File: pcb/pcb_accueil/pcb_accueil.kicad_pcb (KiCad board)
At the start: 2 copper layers, 76 x 32 mm, 5 parts, among them J1 AMP 5- 5530843-4, J2 IDC - Header 2x10

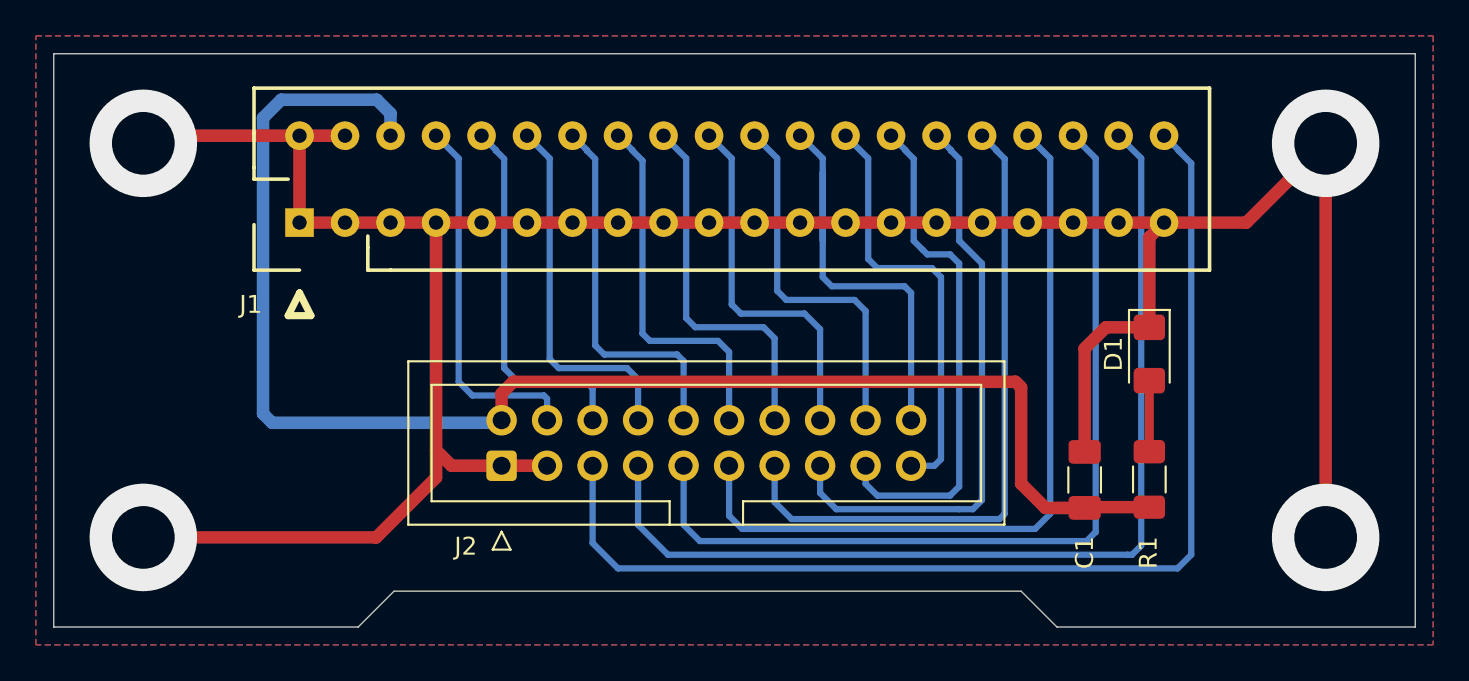
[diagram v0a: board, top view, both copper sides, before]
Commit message: rajout de trous de precage dans pcb_accueil
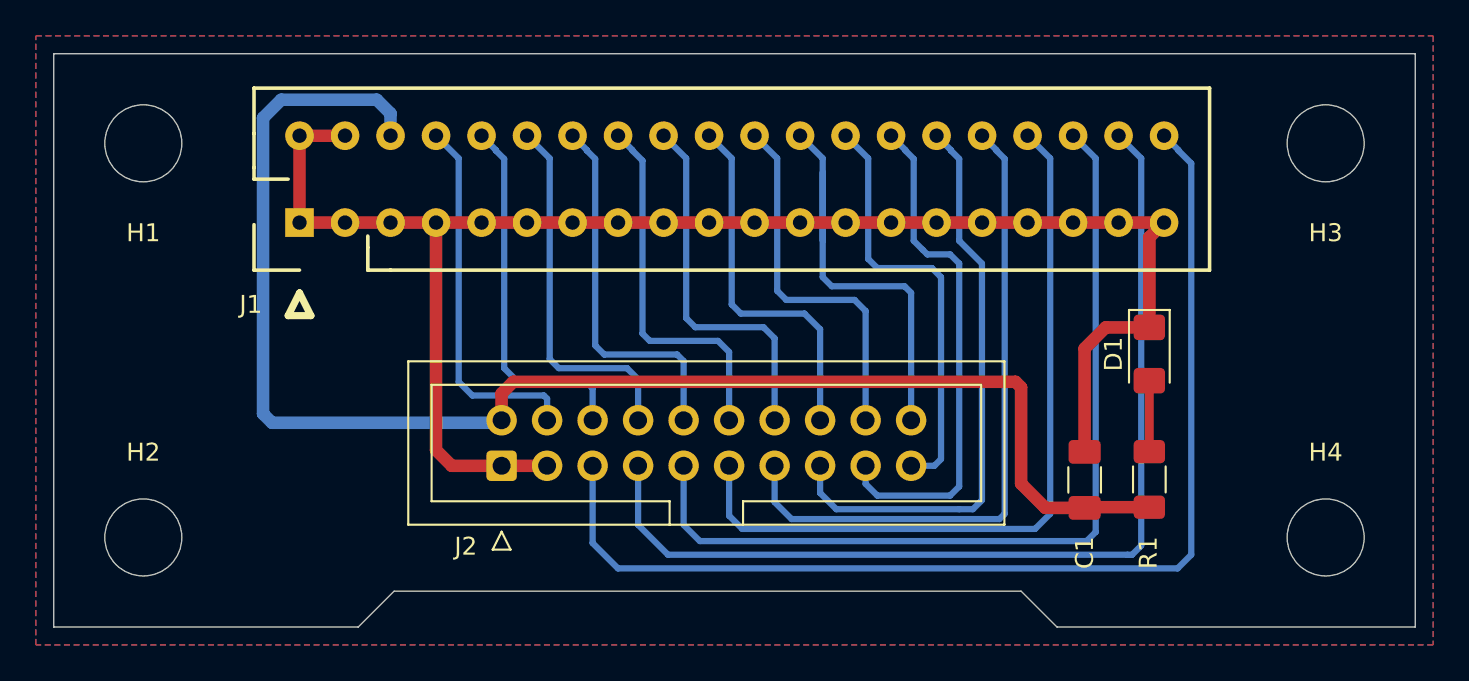
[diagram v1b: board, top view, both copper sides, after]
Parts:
- added H1: MountingHole, MountingHole:MountingHole_4.3mm_M4_DIN965, F.Cu at (116.0, 86.0)
- added H2: MountingHole, MountingHole:MountingHole_4.3mm_M4_DIN965, F.Cu at (116.0, 108.0)
- added H3: MountingHole, MountingHole:MountingHole_4.3mm_M4_DIN965, F.Cu at (182.0, 86.0)
- added H4: MountingHole, MountingHole:MountingHole_4.3mm_M4_DIN965, F.Cu at (182.0, 108.0)
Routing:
- net GND: track 152.0 -> 91.0 mm, vias 4 -> 0
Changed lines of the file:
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@@
     (thickness 1.6)
     (drawings 16)
-    (tracks 170)
+    (tracks 158)
     (zones 0)
-    (modules 5)
+    (modules 9)
     (nets 21)
   )
@@
   )
   (setup
-    (last_trace_width 0.7)
+    (last_trace_width 0.25)
     (user_trace_width 0.25)
     (user_trace_width 0.3)
@@
     (mod_text_size 1 1)
     (mod_text_width 0.15)
-    (pad_size 1.524 1.524)
-    (pad_drill 0.762)
+    (pad_size 4.3 4.3)
+    (pad_drill 4.3)
     (pad_to_mask_clearance 0.051)
     (solder_mask_min_width 0.25)
@@
     )
   )
+  (module MountingHole:MountingHole_4.3mm_M4_DIN965 locked (layer F.Cu)
+    (at 116 86)
+    (descr "Mounting Hole 4.3mm, no annular, M4, DIN965")
+    (tags "mounting hole 4.3mm no annular m4 din965")
+    (attr virtual)
+    (fp_text reference H1 (at 0 5) (layer F.SilkS)
+      (effects (font (size 1 1) (thickness 0.15)))
+    )
+    (fp_text value MountingHole (at 0 4.75) (layer F.Fab)
+      (effects (font (size 1 1) (thickness 0.15)))
+    )
+    (fp_text user %R (at 0.3 0) (layer F.Fab)
+      (effects (font (size 1 1) (thickness 0.15)))
+    )
+    (fp_circle (center 0 0) (end 3.75 0) (layer Cmts.User) (width 0.15))
+    (fp_circle (center 0 0) (end 4 0) (layer F.CrtYd) (width 0.05))
+    (pad 1 np_thru_hole circle (at 0 0) (size 4.3 4.3) (drill 4.3) (layers *.Cu *.Mask))
+  )
+  (module MountingHole:MountingHole_4.3mm_M4_DIN965 locked (layer F.Cu)
+    (at 116 108)
+    (descr "Mounting Hole 4.3mm, no annular, M4, DIN965")
+    (tags "mounting hole 4.3mm no annular m4 din965")
+    (attr virtual)
+    (fp_text reference H2 (at 0 -4.75) (layer F.SilkS)
+      (effects (font (size 1 1) (thickness 0.15)))
+    )
+    (fp_text value MountingHole (at 0 4.75) (layer F.Fab)
+      (effects (font (size 1 1) (thickness 0.15)))
+    )
+    (fp_circle (center 0 0) (end 4 0) (layer F.CrtYd) (width 0.05))
+    (fp_circle (center 0 0) (end 3.75 0) (layer Cmts.User) (width 0.15))
+    (fp_text user %R (at 0.3 0) (layer F.Fab)
+      (effects (font (size 1 1) (thickness 0.15)))
+    )
+    (pad 1 np_thru_hole circle (at 0 0) (size 4.3 4.3) (drill 4.3) (layers *.Cu *.Mask))
+  )
+  (module MountingHole:MountingHole_4.3mm_M4_DIN965 locked (layer F.Cu)
+    (at 182 86)
+    (descr "Mounting Hole 4.3mm, no annular, M4, DIN965")
+    (tags "mounting hole 4.3mm no annular m4 din965")
+    (attr virtual)
+    (fp_text reference H3 (at 0 5) (layer F.SilkS)
+      (effects (font (size 1 1) (thickness 0.15)))
+    )
+    (fp_text value MountingHole (at 0 4.75) (layer F.Fab)
+      (effects (font (size 1 1) (thickness 0.15)))
+    )
+    (fp_text user %R (at 0.3 0) (layer F.Fab)
+      (effects (font (size 1 1) (thickness 0.15)))
+    )
+    (fp_circle (center 0 0) (end 3.75 0) (layer Cmts.User) (width 0.15))
+    (fp_circle (center 0 0) (end 4 0) (layer F.CrtYd) (width 0.05))
+    (pad 1 np_thru_hole circle (at 0 0) (size 4.3 4.3) (drill 4.3) (layers *.Cu *.Mask))
+  )
+  (module MountingHole:MountingHole_4.3mm_M4_DIN965 locked (layer F.Cu)
+    (at 182 108)
+    (descr "Mounting Hole 4.3mm, no annular, M4, DIN965")
+    (tags "mounting hole 4.3mm no annular m4 din965")
+    (attr virtual)
+    (fp_text reference H4 (at 0 -4.75) (layer F.SilkS)
+      (effects (font (size 1 1) (thickness 0.15)))
+    )
+    (fp_text value MountingHole (at 0 4.75) (layer F.Fab)
+      (effects (font (size 1 1) (thickness 0.15)))
+    )
+    (fp_circle (center 0 0) (end 4 0) (layer F.CrtYd) (width 0.05))
+    (fp_circle (center 0 0) (end 3.75 0) (layer Cmts.User) (width 0.15))
+    (fp_text user %R (at 0.3 0) (layer F.Fab)
+      (effects (font (size 1 1) (thickness 0.15)))
+    )
+    (pad 1 np_thru_hole circle (at 0 0) (size 4.3 4.3) (drill 4.3) (layers *.Cu *.Mask))
+  )
   (gr_line (start 128 113) (end 111 113) (layer Edge.Cuts) (width 0.05))
   (gr_line (start 167 113) (end 187 113) (layer Edge.Cuts) (width 0.05))
@@
     (arrow2b (pts (xy 190 128) (xy 188.873496 128.586421)))
   )
-  (via (at 116 108) (size 6) (drill 3.5) (layers F.Cu B.Cu) (net 1))
-  (via (at 116 86) (size 6) (drill 3.5) (layers F.Cu B.Cu) (net 1))
-  (via (at 182 86) (size 6) (drill 3.5) (layers F.Cu B.Cu) (net 1))
-  (via (at 182 108) (size 6) (drill 3.5) (layers F.Cu B.Cu) (net 1))
   (segment (start 127.26 85.575) (end 124.72 85.575) (width 0.7) (layer F.Cu) (net 1))
   (segment (start 124.72 85.575) (end 124.72 90.425) (width 0.7) (layer F.Cu) (net 1))
@@
   (segment (start 169.7255 96.2745) (end 172.158 96.2745) (width 0.7) (layer F.Cu) (net 1))
   (segment (start 168.546 97.454) (end 169.7255 96.2745) (width 0.7) (layer F.Cu) (net 1))
-  (segment (start 116.425 85.575) (end 116 86) (width 0.7) (layer F.Cu) (net 1))
-  (segment (start 124.72 85.575) (end 116.425 85.575) (width 0.7) (layer F.Cu) (net 1))
-  (segment (start 116 108) (end 129 108) (width 0.7) (layer F.Cu) (net 1))
-  (segment (start 132.34 104.66) (end 132.34 103.13) (width 0.7) (layer F.Cu) (net 1))
-  (segment (start 129 108) (end 132.34 104.66) (width 0.7) (layer F.Cu) (net 1))
-  (segment (start 177.575 90.425) (end 182 86) (width 0.7) (layer F.Cu) (net 1))
-  (segment (start 172.98 90.425) (end 177.575 90.425) (width 0.7) (layer F.Cu) (net 1))
-  (segment (start 182 86) (end 182 108) (width 0.7) (layer F.Cu) (net 1))
   (segment (start 129.8 84.334) (end 129.8 85.575) (width 0.7) (layer B.Cu) (net 2))
   (segment (start 129.032 83.566) (end 129.8 84.334) (width 0.7) (layer B.Cu) (net 2))

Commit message: retournement des connecteurs de bords de carte
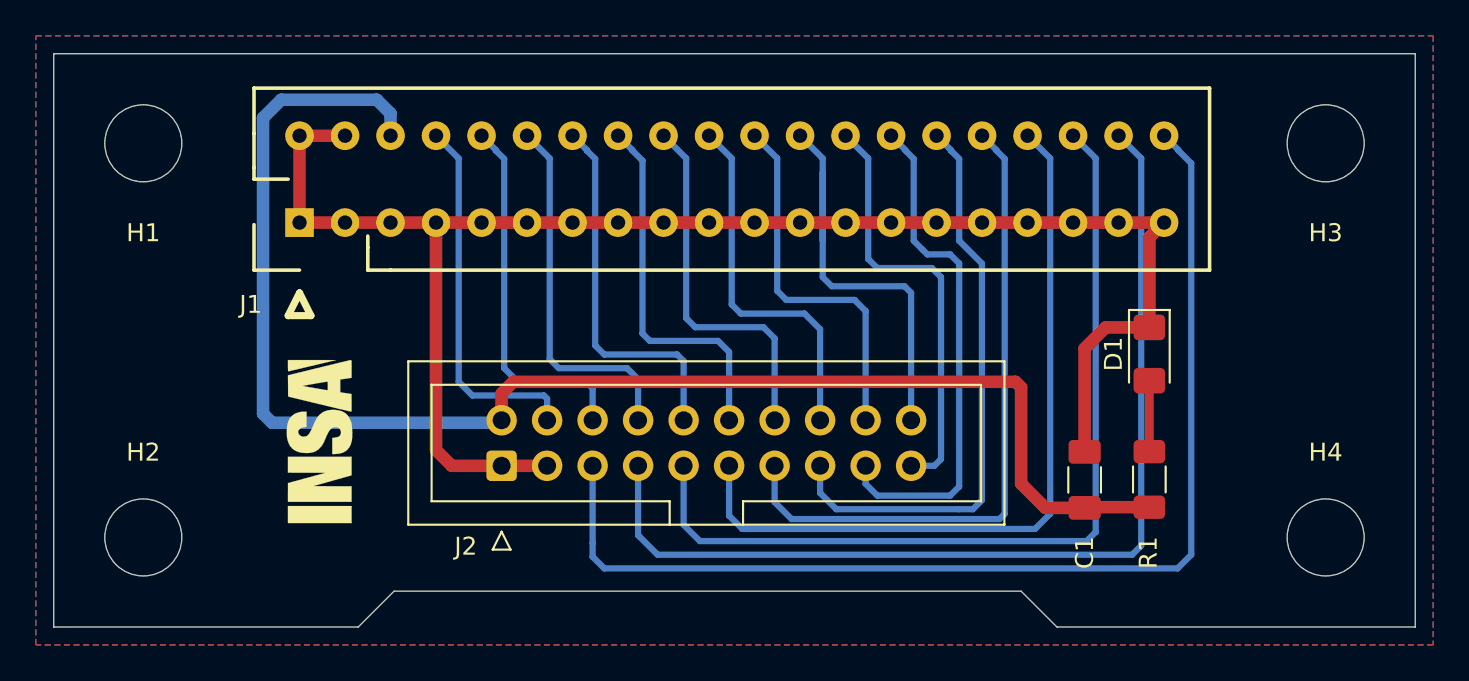
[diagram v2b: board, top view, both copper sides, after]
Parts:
- added G***: LOGO, Insa:insa-image, F.Cu at (126.0, 102.5)

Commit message: Changement d'orientation sur carte-etudiant et pcb_acceuil
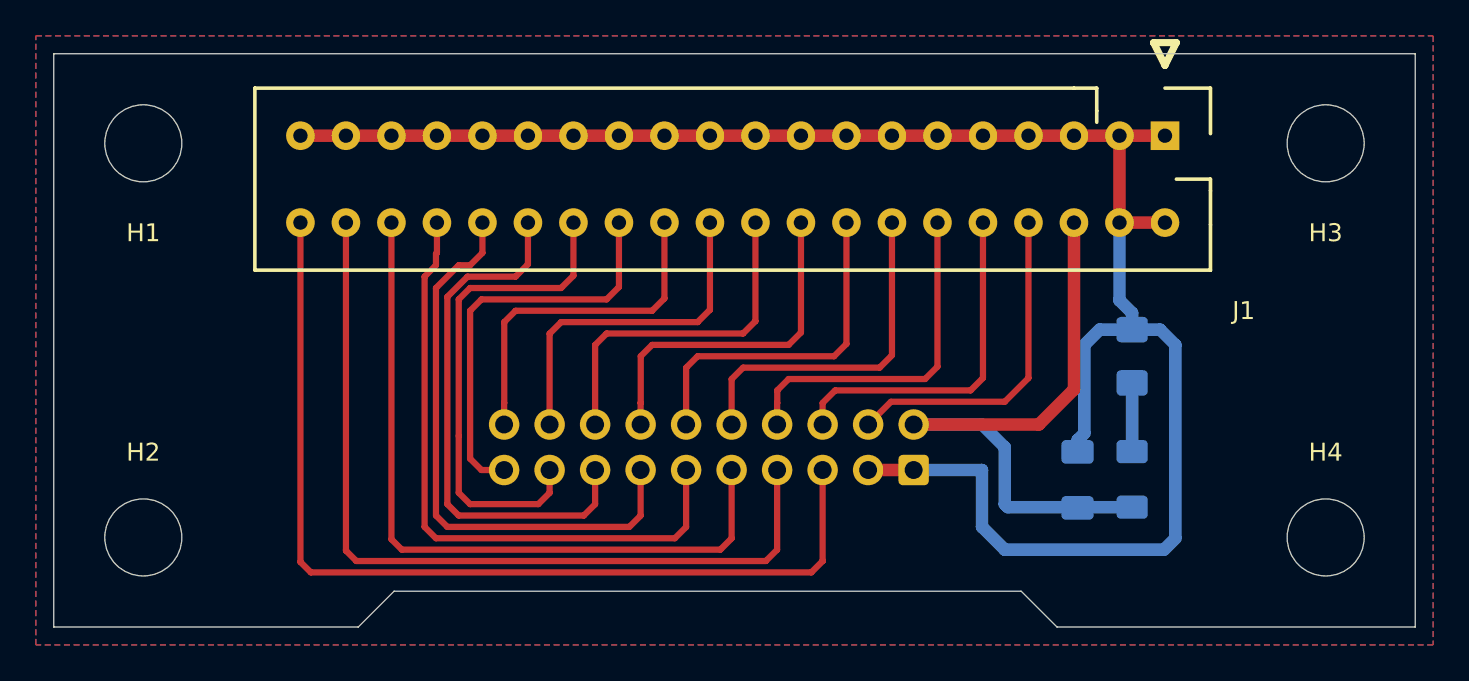
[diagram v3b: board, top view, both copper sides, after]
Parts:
- C1, D1, G***, J2, R1: moved to B.Cu
- moved J2 23.0 mm to (159.0, 104.2)
- moved G*** 22.0 mm to (147.1, 96.4), turned to 180 degrees
- moved J1 12.8 mm to (155.2, 88.0), turned to 180 degrees
- moved D1 0.97 mm to (171.2, 97.9)
- moved R1 0.96 mm to (171.2, 104.8)
- moved C1 0.40 mm to (168.2, 104.8)
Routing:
- net +5V: track 83.2 -> 35.0 mm
- net GND: track 91.0 -> 105.7 mm
- net /RFU: track 63.1 -> 53.7 mm
- net /TENSION_BATTERIE: track 56.0 -> 47.3 mm
- net /DETECTION_CARTE: track 49.5 -> 41.0 mm
- net /GIROUETTE_INDEX: track 43.0 -> 35.6 mm
- net /XBEE_UART_RX: track 24.6 -> 19.4 mm
- net /GIROUETTE_PHA: track 37.0 -> 32.3 mm
- net /GIROUETTE_PHB: track 32.5 -> 29.8 mm
- net /CAPTEUR_SPI_MOSI: track 20.8 -> 18.7 mm
- net /CAPTEUR_CS: track 20.8 -> 19.4 mm
- net /CAPTEUR_SPI_MISO: track 20.7 -> 19.4 mm
- net /SERVO_PWM: track 20.7 -> 19.4 mm
- net /XBEE_UART_TX: track 20.7 -> 19.4 mm
- net /PLATEAU_DIRECTION: track 20.7 -> 19.4 mm
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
